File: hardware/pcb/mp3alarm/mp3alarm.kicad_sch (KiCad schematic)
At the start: 27 parts, among them IC1 RDA5807FP, J0 debug, J1 AUDIO, J10 Conn_Coaxial, J2 SW0, J3 SW1, J4 SW2, J5 I2C, J6 TM1637, J7 microSD, J8 5V, J9 ANT, U1 UDA1334A_Breakout, U2 mini_esp32, Y1 Crystal

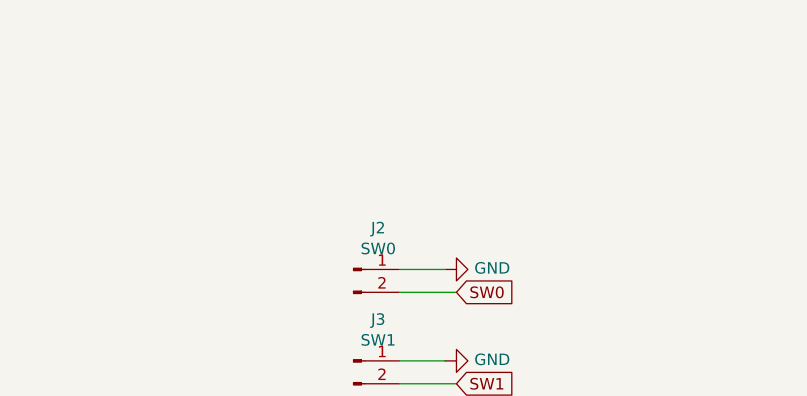
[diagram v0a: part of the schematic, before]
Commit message: * New partition table * Changed to audio pipeline (arduino-audio-tools) * PCB: new sat connector layout * PCB: added pullup resistors for switch pins
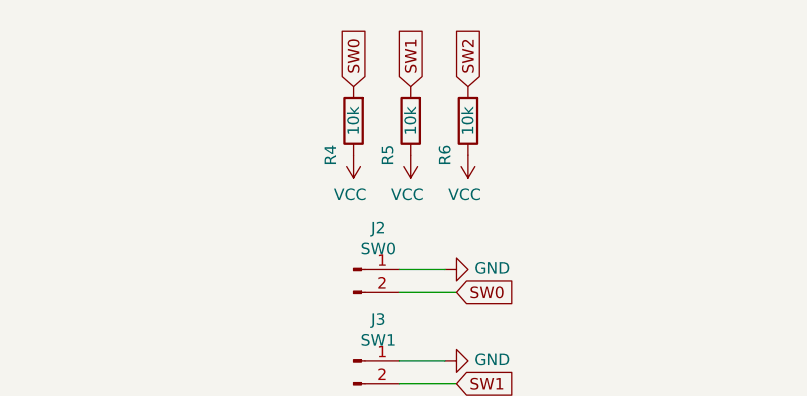
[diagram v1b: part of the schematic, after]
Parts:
- added R4, R5, R6: 10k, Resistor_SMD:R_1206_3216Metric, symbol Device:R
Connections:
- net SW0: now also R4.2
- net SW1: now also R5.2
- net SW2: now also R6.2
- net VCC: now also R4.1, R5.1, R6.1
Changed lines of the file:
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@@
+    )
+  )
+  (global_label "SW0" (shape input) (at 71.12 22.86 90) (fields_autoplaced)
+    (effects (font (size 1.27 1.27)) (justify left))
+    (property "Referenzen zwischen Schaltplänen" "${INTERSHEET_REFS}" (id 0) (at 25.4 105.41 0)
+      (effects (font (size 1.27 1.27)) hide)
     )
   )
@@
     )
   )
+  (global_label "SW2" (shape input) (at 83.82 22.86 90) (fields_autoplaced)
+    (effects (font (size 1.27 1.27)) (justify left))
+    (property "Referenzen zwischen Schaltplänen" "${INTERSHEET_REFS}" (id 0) (at 83.7406 16.6653 90)
+      (effects (font (size 1.27 1.27)) (justify left) hide)
+    )
+  )
   (global_label "SDA" (shape input) (at 229.87 100.33 180) (fields_autoplaced)
     (effects (font (size 1.27 1.27)) (justify right))
@@
     (property "Referenzen zwischen Schaltplänen" "${INTERSHEET_REFS}" (id 0) (at 0 0 0)
       (effects (font (size 1.27 1.27)) hide)
+    )
+  )
+  (global_label "SW1" (shape input) (at 77.47 22.86 90) (fields_autoplaced)
+    (effects (font (size 1.27 1.27)) (justify left))
+    (property "Referenzen zwischen Schaltplänen" "${INTERSHEET_REFS}" (id 0) (at 77.3906 16.6653 90)
+      (effects (font (size 1.27 1.27)) (justify left) hide)
     )
   )
@@
     (pin "1")
   )
+  (symbol (lib_id "Device:R") (at 77.47 26.67 180) (unit 1)
+    (in_bom yes) (on_board yes)
+    (property "Reference" "R5" (id 0) (at 74.93 30.48 90))
+    (property "Value" "10k" (id 1) (at 77.47 26.67 90))
+    (property "Footprint" "Resistor_SMD:R_1206_3216Metric" (id 2) (at 79.248 26.67 90)
+      (effects (font (size 1.27 1.27)) hide)
+    )
+    (property "Datasheet" "~" (id 3) (at 77.47 26.67 0)
+      (effects (font (size 1.27 1.27)) hide)
+    )
+    (pin "1")
+    (pin "2")
+  )
   (symbol (lib_id "Device:R") (at 233.68 110.49 0) (unit 1)
     (in_bom yes) (on_board yes) (fields_autoplaced)
@@
     (pin "4")
   )
+  (symbol (lib_id "power:VCC") (at 71.12 30.48 180) (unit 1)
+    (in_bom yes) (on_board yes)
+    (property "Reference" "#PWR0123" (id 0) (at 71.12 26.67 0)
+      (effects (font (size 1.27 1.27)) hide)
+    )
+    (property "Value" "VCC" (id 1) (at 70.739 34.8742 0))
+    (property "Footprint" "" (id 2) (at 71.12 30.48 0)
+      (effects (font (size 1.27 1.27)) hide)
+    )
+    (property "Datasheet" "" (id 3) (at 71.12 30.48 0)
+      (effects (font (size 1.27 1.27)) hide)
+    )
+    (pin "1")
+  )
+  (symbol (lib_id "power:VCC") (at 77.47 30.48 180) (unit 1)
+    (in_bom yes) (on_board yes)
+    (property "Reference" "#PWR0121" (id 0) (at 77.47 26.67 0)
+      (effects (font (size 1.27 1.27)) hide)
+    )
+    (property "Value" "VCC" (id 1) (at 77.089 34.8742 0))
+    (property "Footprint" "" (id 2) (at 77.47 30.48 0)
+      (effects (font (size 1.27 1.27)) hide)
+    )
+    (property "Datasheet" "" (id 3) (at 77.47 30.48 0)
+      (effects (font (size 1.27 1.27)) hide)
+    )
+    (pin "1")
+  )
+  (symbol (lib_id "power:VCC") (at 83.82 30.48 180) (unit 1)
+    (in_bom yes) (on_board yes)
+    (property "Reference" "#PWR0122" (id 0) (at 83.82 26.67 0)
+      (effects (font (size 1.27 1.27)) hide)
+    )
+    (property "Value" "VCC" (id 1) (at 83.439 34.8742 0))
+    (property "Footprint" "" (id 2) (at 83.82 30.48 0)
+      (effects (font (size 1.27 1.27)) hide)
+    )
+    (property "Datasheet" "" (id 3) (at 83.82 30.48 0)
+      (effects (font (size 1.27 1.27)) hide)
+    )
+    (pin "1")
+  )
   (symbol (lib_id "power:VCC") (at 233.68 114.3 180) (unit 1)
     (in_bom yes) (on_board yes)
@@
     )
     (pin "1")
+  )
+  (symbol (lib_id "Device:R") (at 71.12 26.67 180) (unit 1)
+    (in_bom yes) (on_board yes)
+    (property "Reference" "R4" (id 0) (at 68.58 30.48 90))
+    (property "Value" "10k" (id 1) (at 71.12 26.67 90))
+    (property "Footprint" "Resistor_SMD:R_1206_3216Metric" (id 2) (at 72.898 26.67 90)
+      (effects (font (size 1.27 1.27)) hide)
+    )
+    (property "Datasheet" "~" (id 3) (at 71.12 26.67 0)
+      (effects (font (size 1.27 1.27)) hide)
+    )
+    (pin "1")
+    (pin "2")
+  )
+  (symbol (lib_id "Device:R") (at 83.82 26.67 180) (unit 1)
+    (in_bom yes) (on_board yes)
+    (property "Reference" "R6" (id 0) (at 81.28 30.48 90))
+    (property "Value" "10k" (id 1) (at 83.82 26.67 90))
+    (property "Footprint" "Resistor_SMD:R_1206_3216Metric" (id 2) (at 85.598 26.67 90)
+      (effects (font (size 1.27 1.27)) hide)
+    )
+    (property "Datasheet" "~" (id 3) (at 83.82 26.67 0)
+      (effects (font (size 1.27 1.27)) hide)
+    )
+    (pin "1")
+    (pin "2")
   )
   (symbol (lib_id "Mechanical:MountingHole_Pad") (at 276.86 24.13 0) (unit 1)
@@
       (reference "#PWR0120") (unit 1) (value "GND") (footprint "")
     )
+    (path "/6565db67-38cd-4177-9de9-dc3186b28bf2"
+      (reference "#PWR0121") (unit 1) (value "VCC") (footprint "")
+    )
+    (path "/716bc8da-9918-47b5-93fb-d62f5bad5057"
+      (reference "#PWR0122") (unit 1) (value "VCC") (footprint "")
+    )
+    (path "/4f5bc065-2315-420b-8e33-efeea4d1f5e2"
+      (reference "#PWR0123") (unit 1) (value "VCC") (footprint "")
+    )
     (path "/3be2b67d-91a9-4ca7-9b85-2466808ee9b8"
       (reference "C1") (unit 1) (value "1nF") (footprint "Capacitor_SMD:C_1206_3216Metric")
@@
       (reference "R3") (unit 1) (value "10k") (footprint "Resistor_SMD:R_1206_3216Metric")
     )
+    (path "/d73a9f23-ff09-4cb2-a80f-aba48492760e"
+      (reference "R4") (unit 1) (value "10k") (footprint "Resistor_SMD:R_1206_3216Metric")
+    )
+    (path "/036a88bc-7a6f-4636-9662-4190b023b94b"
+      (reference "R5") (unit 1) (value "10k") (footprint "Resistor_SMD:R_1206_3216Metric")
+    )
+    (path "/d8f9f895-ee6e-4339-9c09-e13fae2f617e"
+      (reference "R6") (unit 1) (value "10k") (footprint "Resistor_SMD:R_1206_3216Metric")
+    )
     (path "/00000000-0000-0000-0000-00005fb9b024"

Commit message: PCB updates
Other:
- moved on the sheet: J10, J9

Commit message: * Latest PCB update for ESP32S3
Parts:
- removed C2: 10uF, Capacitor_SMD:C_Elec_6.3x5.4, symbol Device:C_Polarized_Small
- removed J0: debug, Connector_PinHeader_2.54mm:PinHeader_2x05_P2.54mm_Vertical_SMD, symbol Connector_Generic:Conn_02x05_Odd_Even
- removed J4: SW2, Connector_PinHeader_2.54mm:PinHeader_1x02_P2.54mm_Vertical, symbol Connector:Conn_01x02_Male
- removed R4, R5: 10k, Resistor_SMD:R_1206_3216Metric, symbol Device:R
- removed U1: UDA1334A_Breakout, UDA1334A:UDA1334A-breakout, symbol mp3alarm-rescue:UDA1334A_Breakout-UDA1334A
- removed U2: mini_esp32, pcb:ESP32_mini, symbol mp3alarm-rescue:mini_esp32-ESP32_mini
- added C10, C11, C13, C19: 0.1uF, Capacitor_SMD:C_1206_3216Metric, symbol Device:C_Small
- added C12, C14, C20, C4, C5: 10uF, Capacitor_SMD:C_1206_3216Metric, symbol Device:C_Small
- added C15, C16: 47uF, Capacitor_SMD:C_Elec_6.3x5.4, symbol Device:C_Polarized_Small
- added C17, C18: 0.01uF, Capacitor_SMD:C_1206_3216Metric, symbol Device:C_Small
- added C2, C7: 1uF, Capacitor_SMD:C_1206_3216Metric, symbol Device:C_Small
- added C21: 1nF, Capacitor_SMD:C_1206_3216Metric, symbol Device:C_Small
- added C6: 22uF, Capacitor_SMD:C_1206_3216Metric, symbol Device:C_Small
- added D3: D_Schottky, Diode_SMD:D_0805_2012Metric, symbol Device:D_Schottky
- added D4: PWR, LED_SMD:LED_0805_2012Metric, symbol Device:LED
- added FB1, FB2: FerriteBead_Small, Resistor_SMD:R_0805_2012Metric, symbol Device:FerriteBead_Small
- added J11: USB_C_Receptacle_USB2.0, Connector_USB:USB_C_Receptacle_JAE_DX07S016JA1R1500, symbol Connector:USB_C_Receptacle_USB2.0
- added J4: AudioJack3, footprints:PJ-313, symbol Connector_Audio:AudioJack3
- added R10, R16: 220k, Resistor_SMD:R_1206_3216Metric, symbol Device:R
- added R11, R12, R13, R14, R15, R19, R20, R21, R22, R23, R24, R8: 10k, Resistor_SMD:R_1206_3216Metric, symbol Device:R
- added R17, R18: 100, Resistor_SMD:R_1206_3216Metric, symbol Device:R
- added R7: 5k1, Resistor_SMD:R_1206_3216Metric, symbol Device:R
- added R9: 680, Resistor_SMD:R_1206_3216Metric, symbol Device:R
- added SW1: SW_RST, Button_Switch_SMD:SW_SPST_CK_RS282G05A3, symbol Switch:SW_Push
- added SW2: SW_BOOT, Button_Switch_SMD:SW_SPST_CK_RS282G05A3, symbol Switch:SW_Push
- added U2: UDA1334ATS, Package_SO:SSOP-16_4.4x5.2mm_P0.65mm, symbol Audio:UDA1334ATS
- added U3: ESP32-S3-WROOM-1, PCM_Espressif:ESP32-S3-WROOM-1, symbol PCM_Espressif:ESP32-S3-WROOM-1
- added U4: AMS1117-3.3, Package_TO_SOT_SMD:SOT-223-3_TabPin2, symbol Regulator_Linear:AMS1117-3.3
- C3: value 22nF -> 10uF
- R6: value 10k -> 5k1
- Y1: footprint Crystal:Crystal_C26-LF_D2.1mm_L6.5mm_Horizontal -> Crystal:Crystal_SMD_2012-2Pin_2.0x1.2mm
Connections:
- net ANT: now also IC1.4 (FMIN), C21.2; no longer J10.1 (In), J9.1 (Pin_1)
- net GND: now also C3.1, R6.1, C10.1, C13.2, C14.2, C2.1, C4.1, C5.1, C6.1, C7.1, D4.1 (K), FB1.1, J11.A1 (GND), J11.A12 (GND), J11.B1 (GND), J11.B12 (GND), J11.S1 (SHIELD), R19.1, R20.1, R21.1, R22.1, R23.1, R24.1, R7.1, SW1.2, SW2.2, U2.5 (VSSD), U3.1 (GND), U3.40 (GND), U3.41 (GND), U4.1 (GND); no longer C3.2, J1.2 (Pin_2)
- net I2S_BCLK: now also U2.1 (BCK), U3.38 (GPIO2/TOUCH2/ADC1_CH1)
- net I2S_DIN: now also U2.3 (DATAI), U3.39 (GPIO1/TOUCH1/ADC1_CH0)
- net I2S_LRC: now also U2.2 (WS), U3.35 (MTMS/GPIO42)
- net I2S_MUTE: now also R21.2, U2.8 (MUTE), U3.11 (GPIO18/U1RXD/ADC2_CH7/CLK_OUT3)
- net I2S_RADIO_DOUT: now also U3.17 (GPIO9/TOUCH9/ADC1_CH8/FSPIHD/SUBSPIHD)
- net SCL: now also U3.18 (GPIO10/TOUCH10/ADC1_CH9/FSPICS0/FSPIIO4/SUBSPICS0)
- net SDA: now also U3.19 (GPIO11/TOUCH11/ADC2_CH0/FSPID/FSPIIO5/SUBSPID)
- net SD_CLK: now also U3.22 (GPIO14/TOUCH14/ADC2_CH3/FSPIWP/FSPIDQS/SUBSPIWP)
- net SD_CMD: now also R11.1, U3.23 (GPIO21)
- net STATUS_DATA: now also U3.12 (GPIO8/TOUCH8/ADC1_CH7/SUBSPICS1)
- net SW0: now also U3.33 (MTDO/GPIO40/CLK_OUT2)
- net SW1: now also U3.34 (MTDI/GPIO41/CLK_OUT1)
- net TM_CLK: now also U3.32 (MTCK/GPIO39/CLK_OUT3/SUBSPICS1)
- net TM_DIO: now also U3.31 (GPIO38/FSPIWP/SUBSPIWP)
- net VCC: now also C10.2, C13.1, C14.1, C5.2, C6.2, FB2.2, R11.2, R12.2, R13.2, R14.2, R15.2, R8.1, R9.2, U2.4 (VDDD), U3.2 (3V3), U4.2 (VO); no longer C3.1, D1.1 (VDD), D2.1 (VDD), R6.1
- net OUT_L: now reaches J1.1 (Pin_1)
- net OUT_L: now also C17.1, J4.T, R17.2
- net OUT_R: now reaches J1.3 (Pin_3)
- net OUT_R: now also C18.2, J4.R, R18.2
- net SD_D2: now reaches J7.1 (DAT2)
- net SD_D2: now also R14.1, U3.25 (GPIO48/SPICLK_N/SUBSPICLK_N_DIFF)
- net SD_D1: now reaches J7.8 (DAT1)
- net SD_D1: now also R13.1, U3.20 (GPIO12/TOUCH12/ADC2_CH1/FSPICLK/FSPIIO6/SUBSPICLK)
- net at C1.2: now also J10.1 (In); no longer IC1.4 (FMIN)
- net 5V renamed +5V
- net +5V: now also C3.2, D1.1 (VDD), D2.1 (VDD), C4.2, D3.1 (K), U4.3 (VI)
- net SD_CD renamed SD_D3
- net SD_D3: now also R15.1, U3.24 (GPIO47/SPICLK_P/SUBSPICLK_P_DIFF)
- net SD_DATA0 renamed SD_D0
- net SD_D0: now also R12.1, U3.21 (GPIO13/TOUCH13/ADC2_CH2/FSPIQ/FSPIIO7/SUBSPIQ)
- net SW2: no longer names the net of R6.2
- net SW2: now also J11.A5 (CC1)
- new net: C21.1, J9.1 (Pin_1)
- new net: C7.2, R8.2, SW1.1, U3.3 (EN)
- new net: C11.1, C12.1, FB2.1, U2.13 (VDDA)
- new net: C15.1, U2.14 (VOUTL)
- new net: C15.2, R10.2, R17.1
- new net: R23.2, U2.6 (SYSCLK/PLL1)
- new net: C16.2, R16.1, R18.1
- new net: D3.2 (A), J11.A4 (VBUS), J11.A9 (VBUS), J11.B4 (VBUS), J11.B9 (VBUS)
- new net: R24.2, U2.10 (PLL0)
- new net: R20.2, U2.11 (SFOR0)
- new net: C19.2, C20.2, U2.12 (Vref(DAC))
- new net: C16.1, U2.16 (VOUTR)
- new net: R19.2, U2.7 (SFOR1)
- new net: D4.2 (A), R9.1
- new net: J11.B5 (CC2), R7.2
- new net BOOT: C2.2, SW2.1, U3.27 (GPIO0/BOOT)
- new net GNDA: C11.2, C12.2, C17.2, C18.1, C19.1, C20.1, FB1.2, J1.2 (Pin_2), J4.S, R10.1, R16.2, U2.15 (VSSA)
- new net I2S_DEEM: R22.2, U2.9 (DEEM/CLKOUT), U3.15 (GPIO3/TOUCH3/ADC1_CH2)
- new net UART_RX: U3.36 (U0RXD/GPIO44/CLK_OUT2)
- new net UART_TX: U3.37 (U0TXD/GPIO43/CLK_OUT1)
- new net USB_D+: J11.A6 (D+), J11.B6 (D+), U3.14 (GPIO20/U1CTS/ADC2_CH9/CLK_OUT1/USB_D+)
- new net USB_D-: J11.A7 (D-), J11.B7 (D-), U3.13 (GPIO19/U1RTS/ADC2_CH8/CLK_OUT2/USB_D-)
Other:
- moved on the sheet: C1, D1, D2, H1, H2, H3, H4, IC1, J10, J2, J3, J5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
